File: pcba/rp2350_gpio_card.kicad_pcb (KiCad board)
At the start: 2 copper layers, 26 x 30 mm, 42 parts, among them J1 Conn_01x10_Pin, J2 Conn_01x10_Pin, P1 USB_C_Plug_USB2.0, U1 RP2350_60QFN, U2 W25Q128JVS, U4 AP2127K-3.3, Y1 ABM8-272-T3

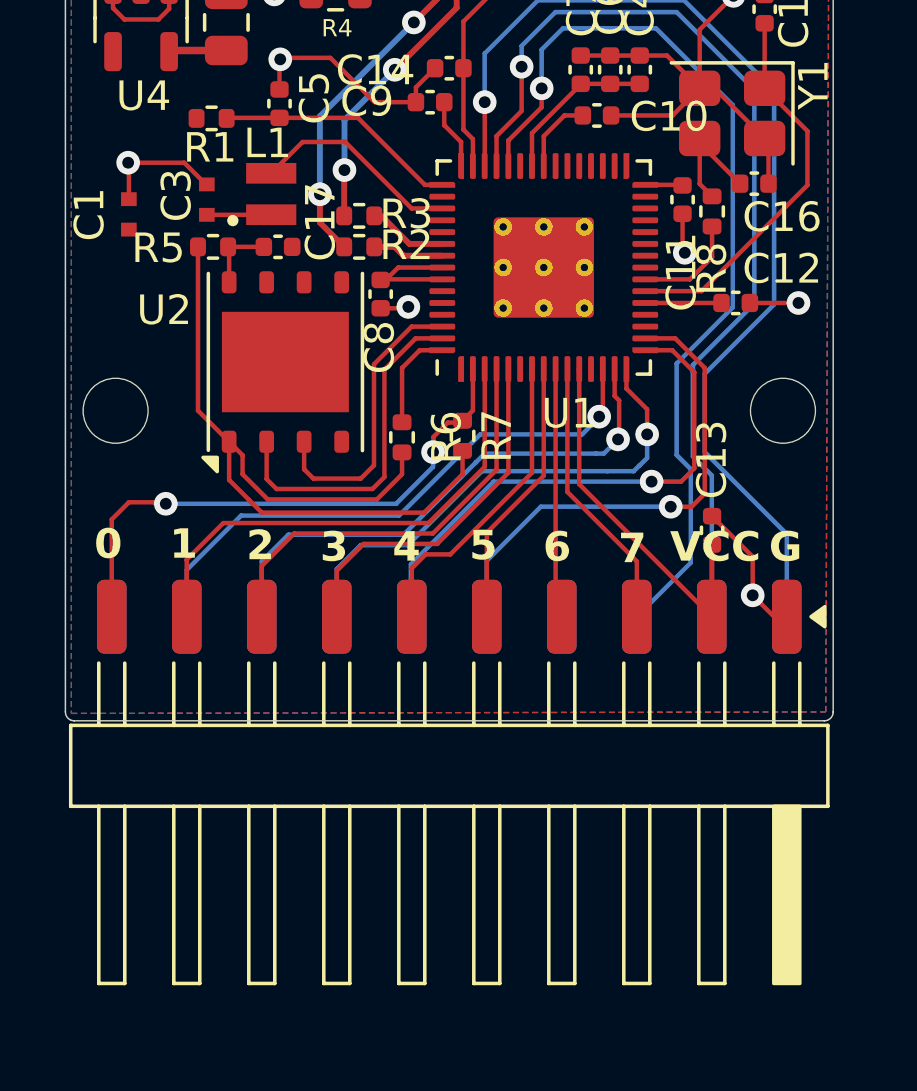
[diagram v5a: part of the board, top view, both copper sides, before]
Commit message: change footprint, version v122
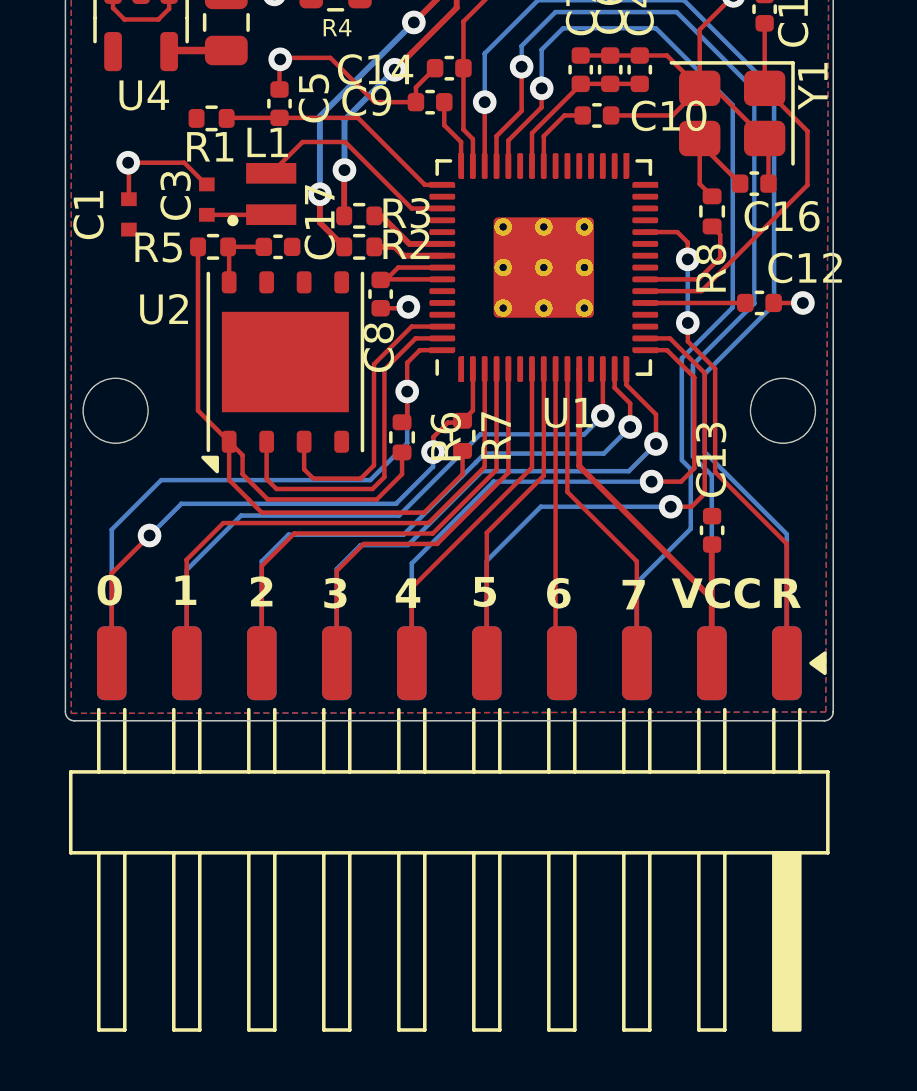
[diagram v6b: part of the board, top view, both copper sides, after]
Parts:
- removed C11: 100n, Capacitor_SMD:C_0402_1005Metric
- moved J1 1.58 mm to (101.1, 88.6)
- moved J2 1.58 mm to (101.1, 88.6)
- moved C12 0.80 mm to (111.6, 70.8)
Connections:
- J1 pad 1: /GPIO8 -> /QSPI_SS
- J1 pad 7: /GPIO26_ADC0 -> GND
- J2 pad 1: GND -> /RUN
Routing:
- net /QSPI_SS: track 3.45 -> 20.9 mm, vias 0 -> 1
- net /RUN: track 0.00 -> 17.2 mm, vias 0 -> 2
- net GND: track 54.9 -> 48.2 mm, vias 16 -> 14
- net /GPIO10: track 18.1 -> 20.0 mm
- net /GPIO11: track 17.0 -> 18.7 mm
- net /GPIO9: track 19.4 -> 21.0 mm
- net /GPIO1: track 16.6 -> 18.2 mm
- net /GPIO7: track 9.36 -> 10.9 mm
- net /GPIO6: track 8.47 -> 10.0 mm
- net /GPIO5: track 9.19 -> 10.8 mm
- net /GPIO3: track 12.3 -> 13.8 mm
- net /GPIO28_ADC2: track 32.9 -> 34.5 mm
- net /GPIO2: track 14.4 -> 16.0 mm
- net /GPIO29_ADC3: track 35.6 -> 37.1 mm
- net /GPIO13: track 16.9 -> 18.4 mm
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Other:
- board text added: "B"
- board text added: "R"
- board text removed: "26"
- board text removed: "8"
